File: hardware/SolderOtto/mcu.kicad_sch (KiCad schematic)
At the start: 27 parts, among them J302 TC-2050, P401 USB_C_Plug_USB2.0, SW302 SW_Push, U301 USBLC6-2SC6, U303 MX25R3235FM1xx0, U304 STM32G474QETx, Y301 32.768 kHz

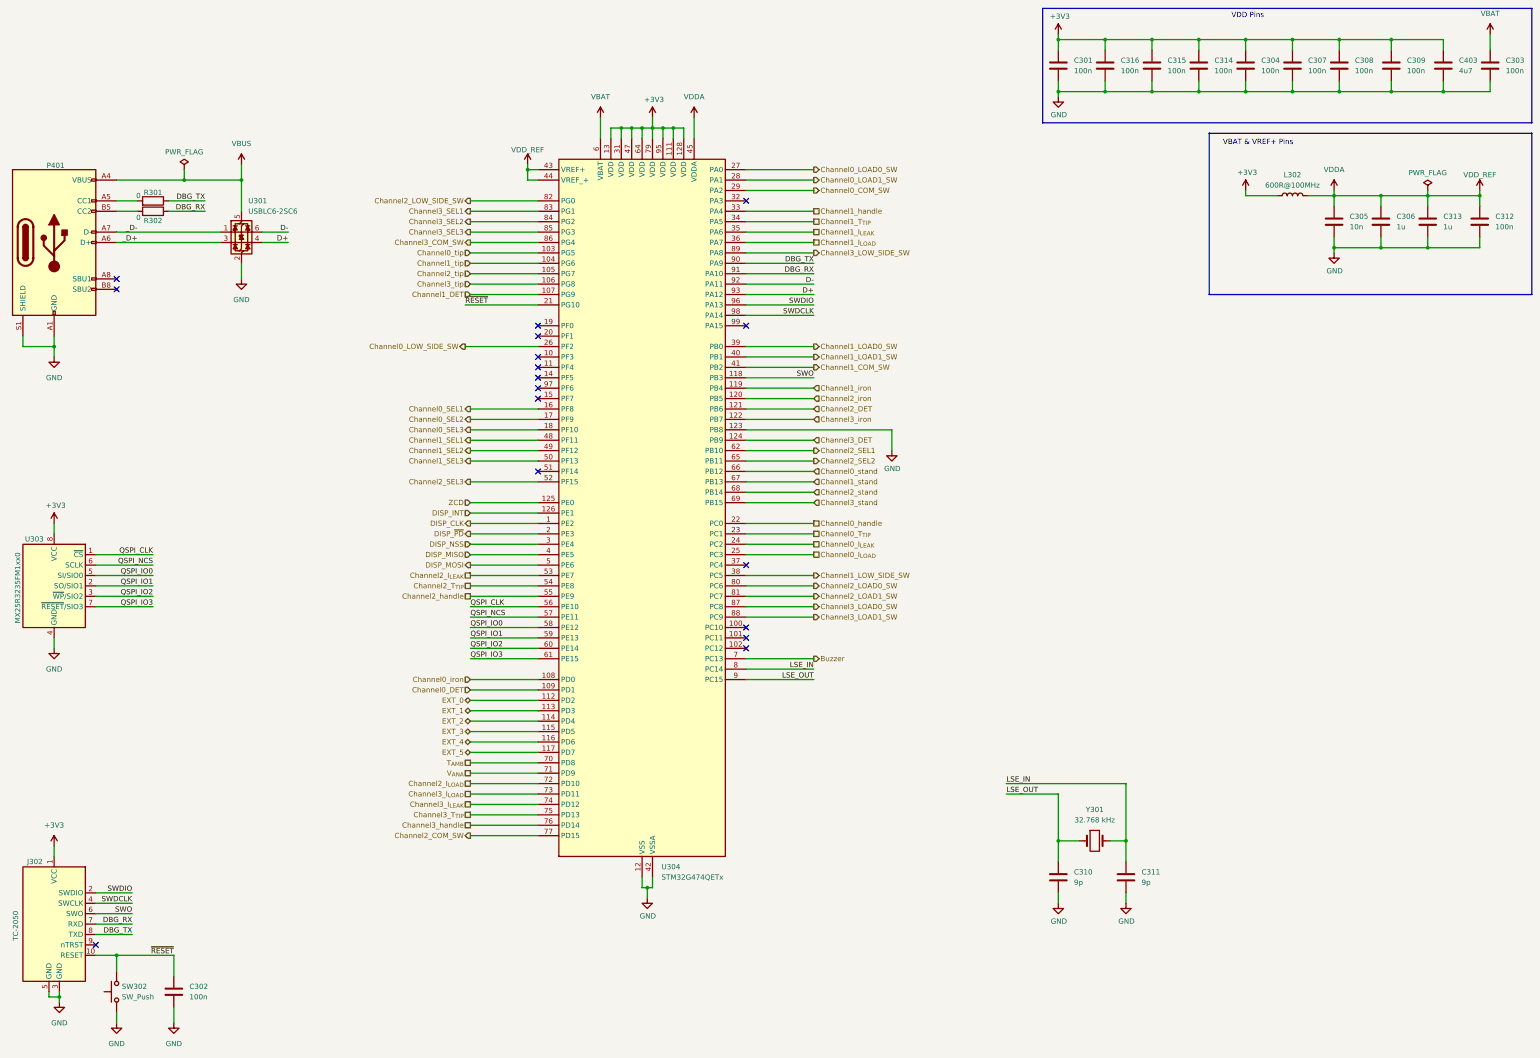
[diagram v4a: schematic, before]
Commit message: create adapter to enclosure for display
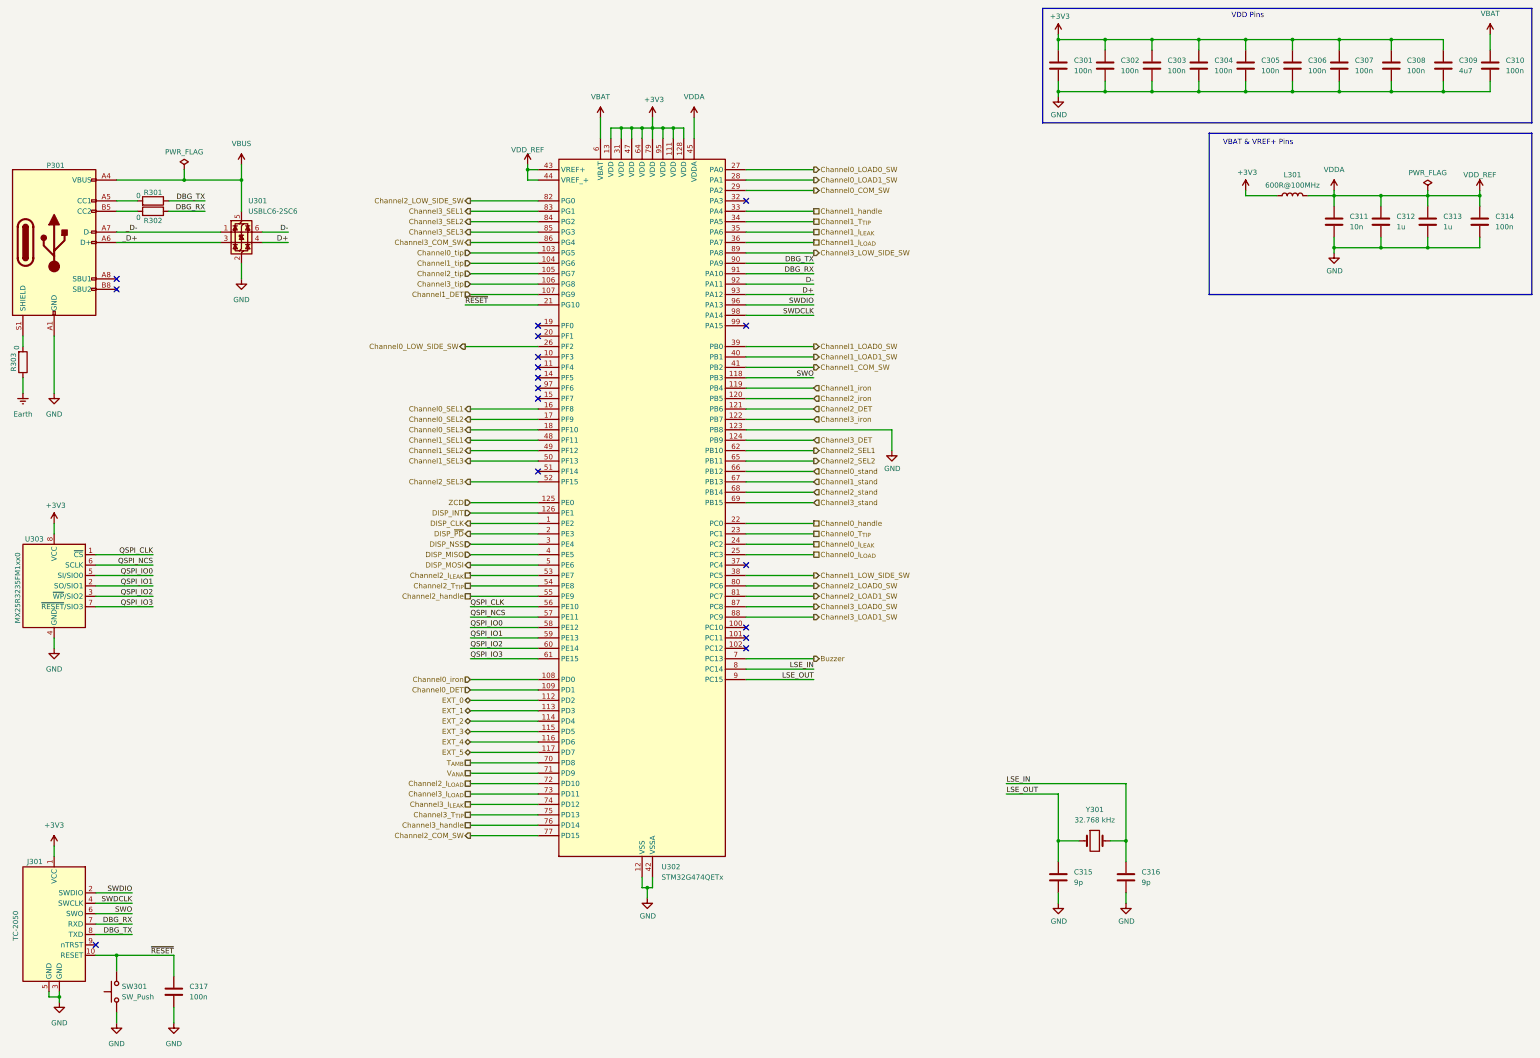
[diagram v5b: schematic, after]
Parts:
- added R303: 0, Resistor_SMD:R_0603_1608Metric, symbol Device:R
- renumbered C316 to C302, C315 to C303, C314 to C304, C304 to C305, C307 to C306, C308 to C307, C309 to C308, C403 to C309, C303 to C310, C305 to C311, C306 to C312, C312 to C314, C310 to C315, C311 to C316, C302 to C317, J302 to J301, L302 to L301, P401 to P301, SW302 to SW301, U304 to U302
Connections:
- net GND: no longer P301.S1 (SHIELD)
- new net: P301.S1 (SHIELD), R303.2
- new net Earth: R303.1

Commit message: save work
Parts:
- added C315: 100n, Capacitor_SMD:C_0603_1608Metric, symbol Device:C
- added C319: 10n, Capacitor_SMD:C_0603_1608Metric, symbol Device:C
- C316: renamed from C315; footprint Capacitor_SMD:C_0603_1608Metric -> Capacitor_SMD:C_0402_1005Metric
- C317: renamed from C316; footprint Capacitor_SMD:C_0603_1608Metric -> Capacitor_SMD:C_0402_1005Metric
- R303: value 0 -> 1M; Digikey (none) -> P1.00MHCT-ND
- U303: footprint Package_SO:SOP-8_3.9x4.9mm_P1.27mm -> Package_SO:SOIC-8_3.9x4.9mm_P1.27mm; Digikey (none) -> MX25R3235FM1IL0-ND
- renumbered C317 to C318
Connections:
- net VBAT is gone; now on net +3V3: C310.1, U302.6 (VBAT)
- net +3V3: now also C315.1
- net Earth: now also R303.2, C319.1; no longer R303.1
- net GND: now also C315.2
- net at P301.S1 (SHIELD): now also R303.1, C319.2; no longer R303.2

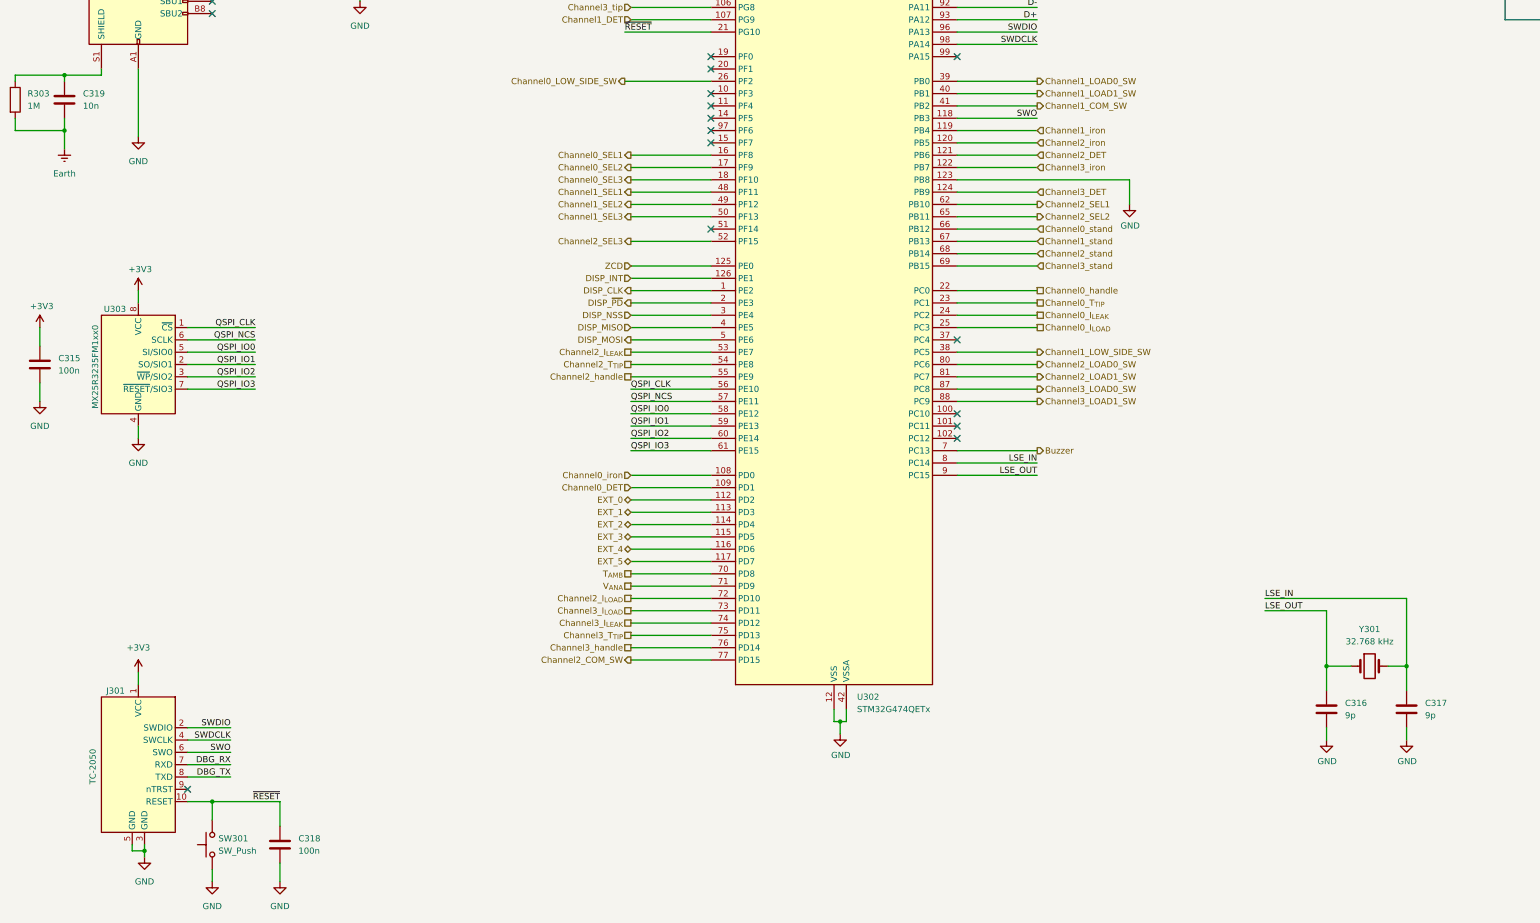
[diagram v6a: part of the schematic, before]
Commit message: try to replace op07c
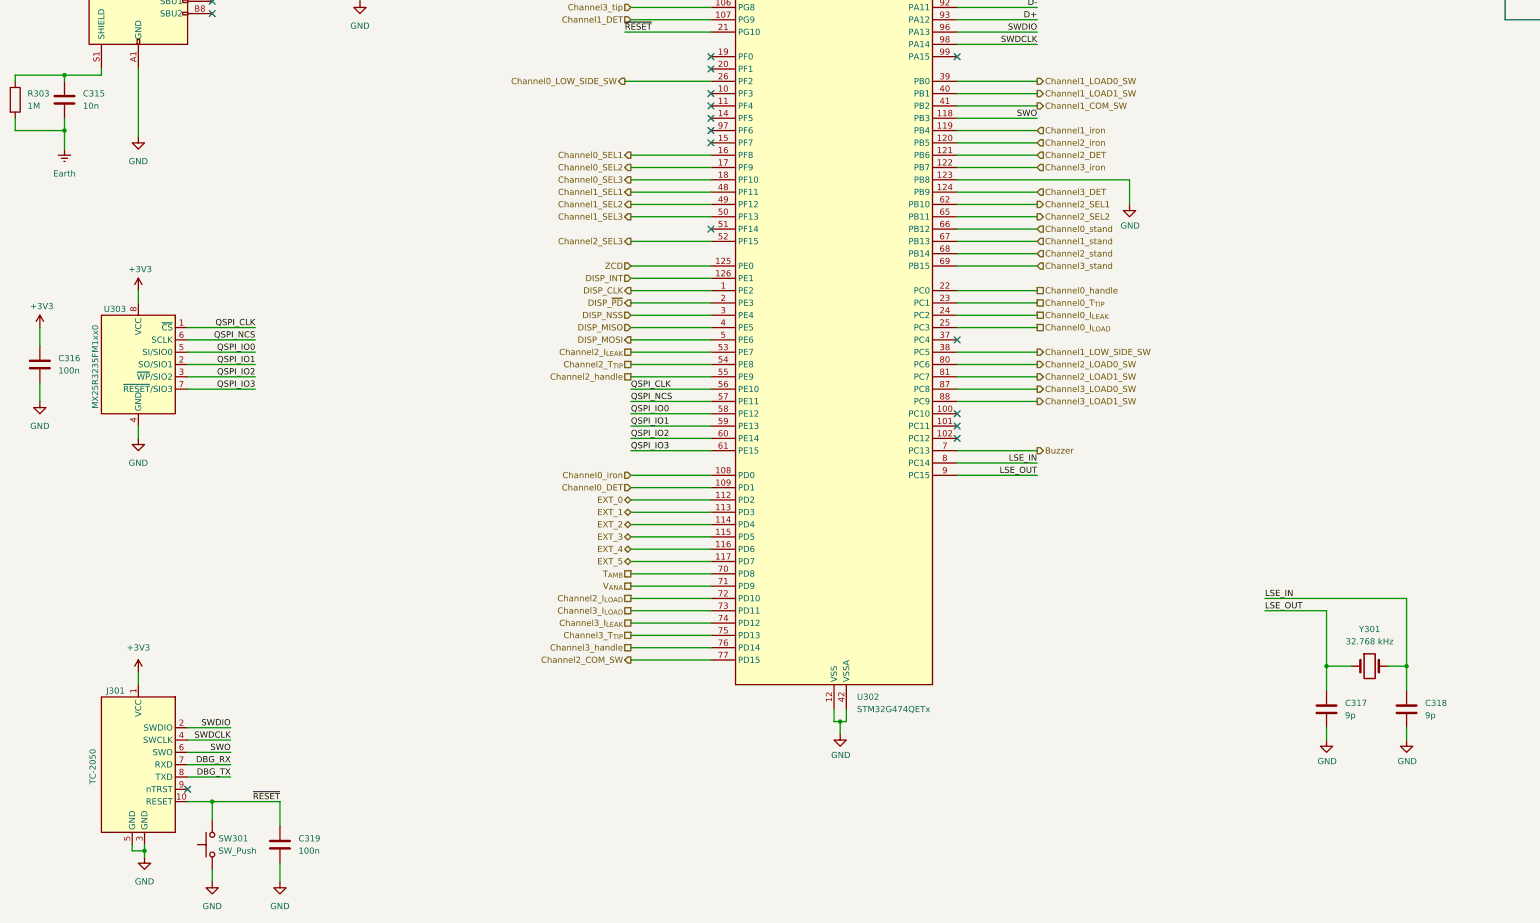
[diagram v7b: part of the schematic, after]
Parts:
- U303: footprint Package_SO:SOIC-8_3.9x4.9mm_P1.27mm -> Package_SO:SOP-8_3.9x4.9mm_P1.27mm
- renumbered C319 to C315, C315 to C316, C316 to C317, C317 to C318, C318 to C319

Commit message: layout finished
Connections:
- net Channel0_COM_SW: now also U302.27 (PA0); no longer U302.29 (PA2)
- net Channel0_I_{LEAK}: now also U302.25 (PC3); no longer U302.24 (PC2)
- net Channel0_I_{LOAD}: now also U302.22 (PC0); no longer U302.25 (PC3)
- net Channel0_LOAD0_SW: now also U302.28 (PA1); no longer U302.27 (PA0)
- net Channel0_LOAD1_SW: now also U302.29 (PA2); no longer U302.28 (PA1)
- net Channel0_T_{TIP}: now also U302.24 (PC2); no longer U302.23 (PC1)
- net Channel0_handle: now also U302.23 (PC1); no longer U302.22 (PC0)
